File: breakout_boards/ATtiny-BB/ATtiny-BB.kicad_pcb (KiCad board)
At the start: 2 copper layers, 52.1 x 10.2 mm, 9 parts, among them J1 Conn_01x04, J2 Conn_01x04, J3 Conn_01x02, J4 AVR-ISP-6, SW1 SW_Push, U1 ATTINY45-20PU

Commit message: Finished the layout
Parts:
- added REF***: OSHW-Logo2_7.3x6mm_SilkScreen, Symbols:OSHW-Logo2_7.3x6mm_SilkScreen, B.Cu at (148.9, 118.6)
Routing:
- net /GND: track 0.00 -> 52.3 mm, vias 0 -> 2
- net /PB0: track 0.00 -> 45.4 mm
- net /PB1: track 0.00 -> 43.2 mm, vias 0 -> 2
- net /PB2: track 0.00 -> 31.9 mm, vias 0 -> 2
- net /PB5: track 0.00 -> 29.1 mm, vias 0 -> 1
- net /VCC: track 0.00 -> 22.9 mm
- net /VCC_in: track 0.00 -> 13.5 mm
- net /PB4: track 0.00 -> 13.1 mm
- net /PB3: track 0.00 -> 12.6 mm, vias 0 -> 1
- net Net-(R1-Pad2): track 0.00 -> 7.38 mm, vias 0 -> 1
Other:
- net class Default: via_drill 0.4 -> 0.3
- net class Power: via_drill 0.4 -> 0.3
- board text added: "ATtiny-BB"
- board text added: "Bottom"
- board text added: "OHL v1.2"
- board text added: "Rev. 18/1"
- board text added: "Top"
- board text added: "http://michis-pla.net"

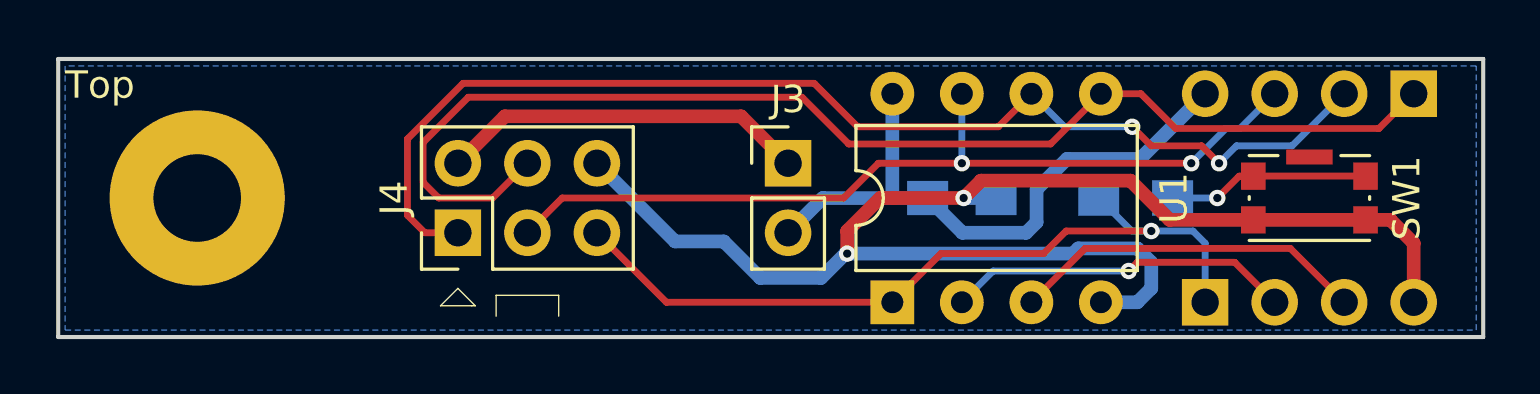
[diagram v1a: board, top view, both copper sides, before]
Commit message: Reduced the size of the PCB a bit.
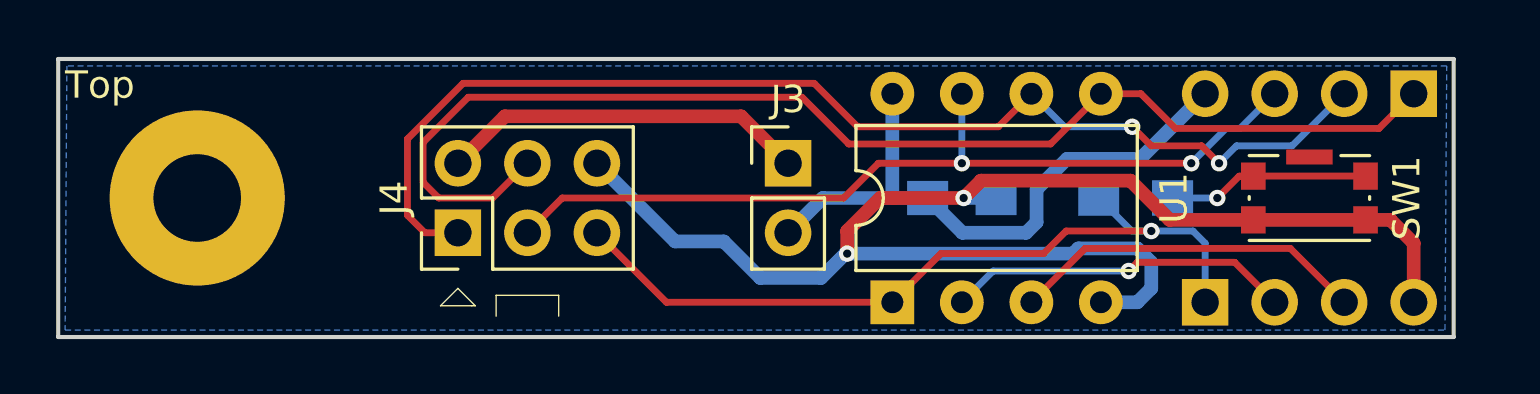
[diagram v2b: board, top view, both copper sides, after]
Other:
- board size 52.1 x 10.2 mm -> 51 x 10.2 mm
- board text added: "Rev. 18/2"
- board text removed: "Rev. 18/1"
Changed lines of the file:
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@@
     (links 22)
     (no_connects 0)
-    (area 119.467143 109.55238 180.568201 126.667619)
+    (area 125.654999 112.954999 176.795501 123.265001)
     (thickness 1.6)
     (drawings 25)
@@
   (title_block
     (title ATtiny-BB)
-    (date 2018-09-02)
-    (rev 1)
+    (date 2018-09-15)
+    (rev 18/2)
     (company "Michael Bemmerl")
     (comment 1 "Open Hardware: CERN OHL v1.2")
@@
     (effects (font (size 1 1) (thickness 0.15)))
   )
-  (gr_text "Rev.\n18/1" (at 176.8475 118.11) (layer B.SilkS)
+  (gr_text "Rev.\n18/2" (at 175.8315 118.11) (layer B.SilkS)
     (effects (font (size 1 1) (thickness 0.15)) (justify left mirror))
   )
@@
   (gr_line (start 135.255 122.428) (end 150.495 122.428) (angle 90) (layer F.CrtYd) (width 0.05))
   (gr_line (start 135.255 113.792) (end 150.495 113.792) (angle 90) (layer F.CrtYd) (width 0.05))
-  (gr_line (start 125.73 123.19) (end 177.8 123.19) (angle 90) (layer Edge.Cuts) (width 0.15))
+  (gr_line (start 125.73 123.19) (end 176.7205 123.19) (angle 90) (layer Edge.Cuts) (width 0.15))
   (gr_line (start 125.73 113.03) (end 125.73 123.19) (angle 90) (layer Edge.Cuts) (width 0.15))
-  (gr_line (start 177.8 113.03) (end 125.73 113.03) (angle 90) (layer Edge.Cuts) (width 0.15))
-  (gr_line (start 177.8 123.19) (end 177.8 113.03) (angle 90) (layer Edge.Cuts) (width 0.15))
+  (gr_line (start 176.7205 113.03) (end 125.73 113.03) (angle 90) (layer Edge.Cuts) (width 0.15))
+  (gr_line (start 176.7205 123.19) (end 176.7205 113.03) (angle 90) (layer Edge.Cuts) (width 0.15))
   (segment (start 168.0845 118.11) (end 166.45 118.11) (width 0.25) (layer B.Cu) (net 1))
   (via (at 168.0845 118.11) (size 0.6) (drill 0.3) (layers F.Cu B.Cu) (net 1))
@@
     (polygon
       (pts
-        (xy 125.984 113.284) (xy 125.984 122.936) (xy 177.546 122.936) (xy 177.546 113.284)
+        (xy 126.0475 113.284) (xy 125.984 122.936) (xy 176.403 122.936) (xy 176.4665 113.284)
       )
     )

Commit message: Fixed update to KiCad 5.
Well, the update didn't quite work out of the box. My footprint library table was still using the KiCad 4 footprints.
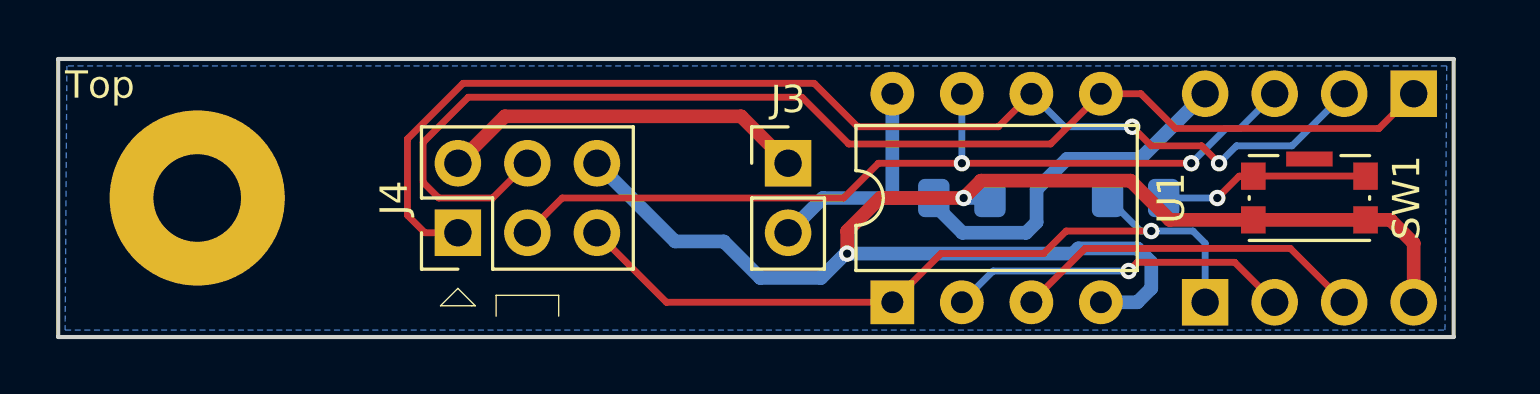
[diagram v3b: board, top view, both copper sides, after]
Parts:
- C1: footprint Capacitors_SMD:C_0805_HandSoldering -> Capacitor_SMD:C_0805_2012Metric_Pad1.15x1.40mm_HandSolder
- J1, J2: footprint Pin_Headers:Pin_Header_Straight_1x04_Pitch2.54mm -> Connector_PinHeader_2.54mm:PinHeader_1x04_P2.54mm_Vertical
- J3: footprint Pin_Headers:Pin_Header_Straight_1x02_Pitch2.54mm -> Connector_PinHeader_2.54mm:PinHeader_1x02_P2.54mm_Vertical
- J4: footprint Pin_Headers:Pin_Header_Straight_2x03_Pitch2.54mm -> Connector_PinHeader_2.54mm:PinHeader_2x03_P2.54mm_Vertical
- R1: footprint Resistors_SMD:R_0805_HandSoldering -> Resistor_SMD:R_0805_2012Metric_Pad1.15x1.40mm_HandSolder
- SW1: footprint Buttons_Switches_SMD:SW_SPST_KMR2_GNDPad -> mibe:SW_Push_1P1T_NO_CK_KMR2_GNDPad
- U1: footprint Housings_DIP:DIP-8_W7.62mm -> Package_DIP:DIP-8_W7.62mm
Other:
- board text added: "Rev. 19/3"
- board text removed: "Rev. 18/2"
